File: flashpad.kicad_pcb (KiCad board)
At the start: 2 copper layers, 61.2 x 65.3 mm, 23 parts, among them U1 ATmega328P-PU, U2 ATmega32A-PU

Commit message: rev2
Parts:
- removed BOOT: BOOT, Button_Switch_THT:SW_PUSH_6mm
- removed the C3 at (155.2, 110.2)
- removed C4, C5: 100n, Capacitor_THT:C_Disc_D5.0mm_W2.5mm_P2.50mm
- removed C6, C7: 22p, Capacitor_THT:C_Disc_D5.0mm_W2.5mm_P5.00mm
- removed ISP1: AVR-ISP-6, Connector_PinHeader_2.54mm:PinHeader_2x03_P2.54mm_Horizontal
- removed LED1: LED, LED_THT:LED_D3.0mm
- removed the R5 at (138.4, 114.0)
- removed RESET: RESET, Button_Switch_THT:SW_PUSH_6mm
- removed XTAL1: Crystal, Crystal:Crystal_HC49-4H_Vertical
- added ACT: LED, LED_THT:LED_D5.0mm, F.Cu at (150.7, 90.1)
- added AVR: AVR-ISP-10, Connector_PinHeader_2.54mm:PinHeader_2x05_P2.54mm_Vertical, F.Cu at (134.7, 143.2)
- added C1: 22p, Capacitor_THT:C_Disc_D5.0mm_W2.5mm_P5.00mm, F.Cu at (100.2, 83.8)
- added C10: 22p, Capacitor_THT:C_Disc_D5.0mm_W2.5mm_P5.00mm, F.Cu at (126.8, 111.1)
- added C11: 22p, Capacitor_THT:C_Disc_D5.0mm_W2.5mm_P5.00mm, F.Cu at (126.8, 127.1)
- added C8: 100n, Capacitor_THT:C_Disc_D5.0mm_W2.5mm_P2.50mm, F.Cu at (128.8, 71.0)
- added C9: 100n, Capacitor_THT:C_Disc_D5.0mm_W2.5mm_P2.50mm, F.Cu at (126.4, 84.8)
- added G***: LOGO, custom_parts:elmo, B.Cu at (102.3, 63.4)
- added G***: LOGO, custom_parts:oshw, F.Cu at (102.2, 63.3)
- added JP1: SelfProg, Connector_PinHeader_2.54mm:PinHeader_1x02_P2.54mm_Vertical, F.Cu at (151.1, 79.9)
- added JP2: SlowSCK, Connector_PinHeader_2.54mm:PinHeader_1x02_P2.54mm_Vertical, F.Cu at (151.0, 75.4)
- added PWR: LED, LED_THT:LED_D5.0mm, F.Cu at (142.2, 90.1)
- added R1: 10k, Resistor_THT:R_Axial_DIN0204_L3.6mm_D1.6mm_P7.62mm_Horizontal, F.Cu at (153.3, 61.0)
- added R10: 1.5K, Resistor_THT:R_Axial_DIN0204_L3.6mm_D1.6mm_P7.62mm_Horizontal, F.Cu at (135.6, 92.3)
- added R2: 270r, Resistor_THT:R_Axial_DIN0204_L3.6mm_D1.6mm_P7.62mm_Horizontal, F.Cu at (123.9, 92.3)
- added R3: 270r, Resistor_THT:R_Axial_DIN0204_L3.6mm_D1.6mm_P7.62mm_Horizontal, F.Cu at (129.6, 92.3)
- added R9: 1.5K, Resistor_THT:R_Axial_DIN0204_L3.6mm_D1.6mm_P7.62mm_Horizontal, F.Cu at (132.7, 92.3)
- added U1: ATmega8A-PU, Package_DIP:DIP-28_W7.62mm, F.Cu at (145.3, 74.2)
- added X1: 12Mhz, Crystal:Crystal_HC49-4H_Vertical, F.Cu at (105.6, 80.0)
- added X2: 16Mhz, Crystal:Crystal_HC49-4H_Vertical, F.Cu at (129.4, 116.7)
- C2: value 100n -> 22p; footprint Capacitor_THT:C_Disc_D5.0mm_W2.5mm_P2.50mm -> Capacitor_THT:C_Disc_D5.0mm_W2.5mm_P5.00mm
- R4: value 1.5K -> 270r
- R5: renamed from R1; value 1.5K -> 2.2k
- U2: footprint Package_DIP:DIP-40_W15.24mm_Socket -> Socket:DIP_Socket-40_W11.9_W12.7_W15.24_W17.78_W18.5_3M_240-1280-00-0602J
- U3: renamed from U1; footprint Package_DIP:DIP-28_W7.62mm_Socket -> custom_parts:DIP_Socket-28_flipped
- USB1: value USB_B_Mini -> USB_B; footprint custom_parts:USB_Mini -> Connector_USB:USB_B_OST_USB-B1HSxx_Horizontal
- moved C2 54.6 mm to (100.2, 71.3)
- moved U3 47.1 mm to (152.8, 138.7), turned to 180 degrees
- moved R4 40.5 mm to (126.8, 92.3), turned to 270 degrees
- moved R6 36.8 mm to (150.5, 61.0)
- moved R5 35.4 mm to (145.0, 68.6)
- moved F1 35.4 mm to (110.9, 62.5), turned to 0 degrees
- moved C3 35.0 mm to (113.6, 67.4), turned to 270 degrees
- moved R7 34.5 mm to (147.7, 61.0)
- moved D2 32.2 mm to (142.0, 68.7)
- moved D1 32.0 mm to (138.8, 68.7)
- moved USB1 15.0 mm to (125.5, 64.7), turned to 90 degrees
- moved U2 1.56 mm to (116.2, 141.7)
- renumbered C1 to C3, R2 to R6, R3 to R7
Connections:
- net XTAL1 renamed XTAL2_1
- net XTAL2 renamed XTAL2_2
- C2 pad 1: +5V -> XTAL1_2
- R4 pad 1: RESET -> Net-(R4-Pad1)
- R4 pad 2: +5V -> SCK
- U2 pad 16: D+ -> Net-(U2-Pad16)
- U2 pad 17: D- -> Net-(U2-Pad17)
- U2 pad 18: BOOT -> Net-(U2-Pad18)
- U2 pad 5: MOSI -> Net-(U2-Pad5)
- U2 pad 6: MISO -> MOSI
- U2 pad 7: SCK -> MISO
- U2 pad 8: Net-(U2-Pad8) -> SCK
- U3 pad 4: D+ -> Net-(U3-Pad4)
- U3 pad 5: D- -> Net-(U3-Pad5)
- U3 pad 6: BOOT -> Net-(U3-Pad6)
- USB1 pad 4: Net-(USB1-Pad4) -> GND
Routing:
- net +5V: track 143.7 -> 259.3 mm
- net BOOT: track 103.5 -> 0.00 mm
- net MISO: track 89.0 -> 169.8 mm
- net Net-(JP1-Pad1): track 0.00 -> 41.5 mm
- net MOSI: track 94.1 -> 135.5 mm
- net RESET: track 93.7 -> 132.8 mm
- net SCK: track 87.3 -> 120.0 mm
- net XTAL1_1: track 0.00 -> 28.9 mm
- net XTAL1_2: track 0.00 -> 27.3 mm
- net LED2: track 0.00 -> 24.0 mm
- net Net-(LED2-Pad1): track 0.00 -> 20.0 mm
- net Net-(R3-Pad1): track 0.00 -> 17.7 mm
- net D-: track 29.8 -> 47.1 mm
- net D+: track 30.6 -> 47.7 mm
- net LED1: track 0.00 -> 16.8 mm
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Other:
- board size 61.2 x 65.3 mm -> 61.3 x 101.4 mm
- rule pad_to_mask_clearance: 0.05 -> 0
- board text added: "USBasp MultiPad by kb-elmo github.com/kb_elmo"

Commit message: update
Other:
- board text added: "USBasp MultiPad by kb-elmo github.com/kb-elmo"
- board text removed: "USBasp MultiPad by kb-elmo github.com/kb_elmo"

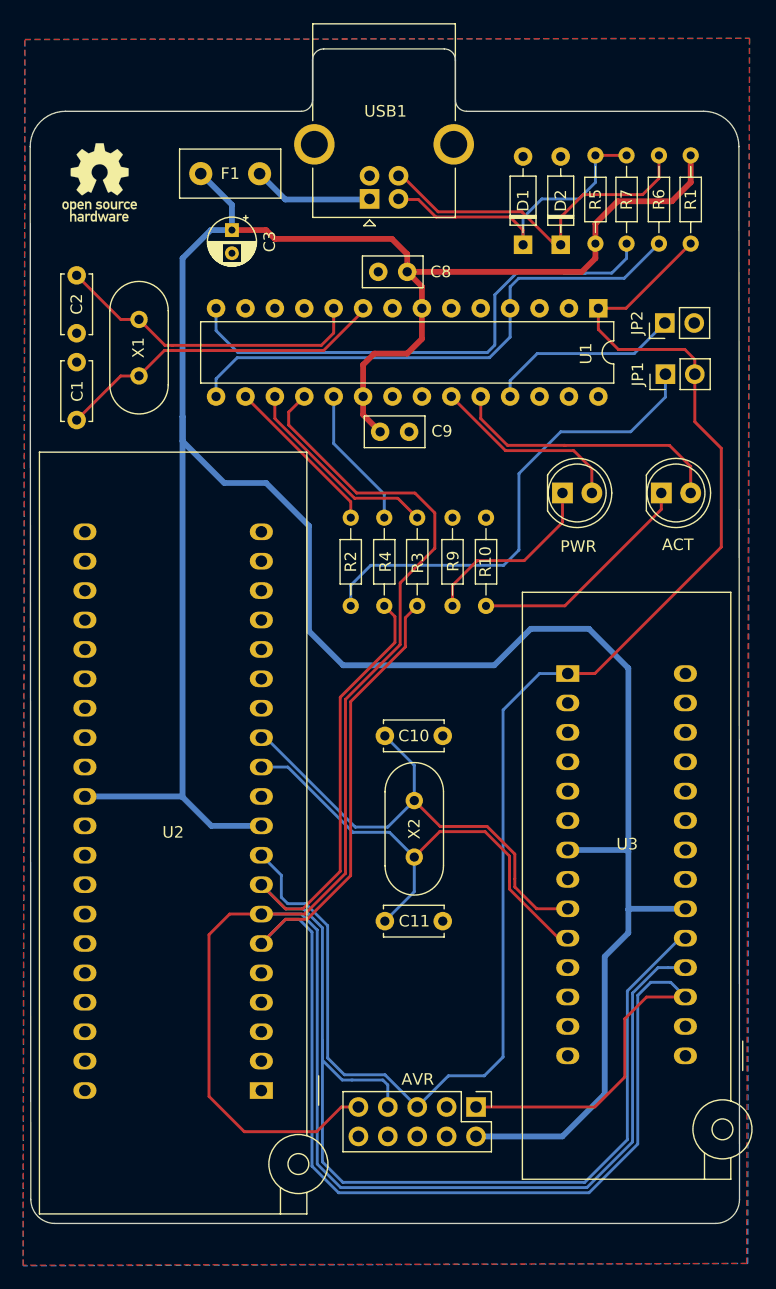
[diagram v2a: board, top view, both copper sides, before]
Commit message: fix footprints
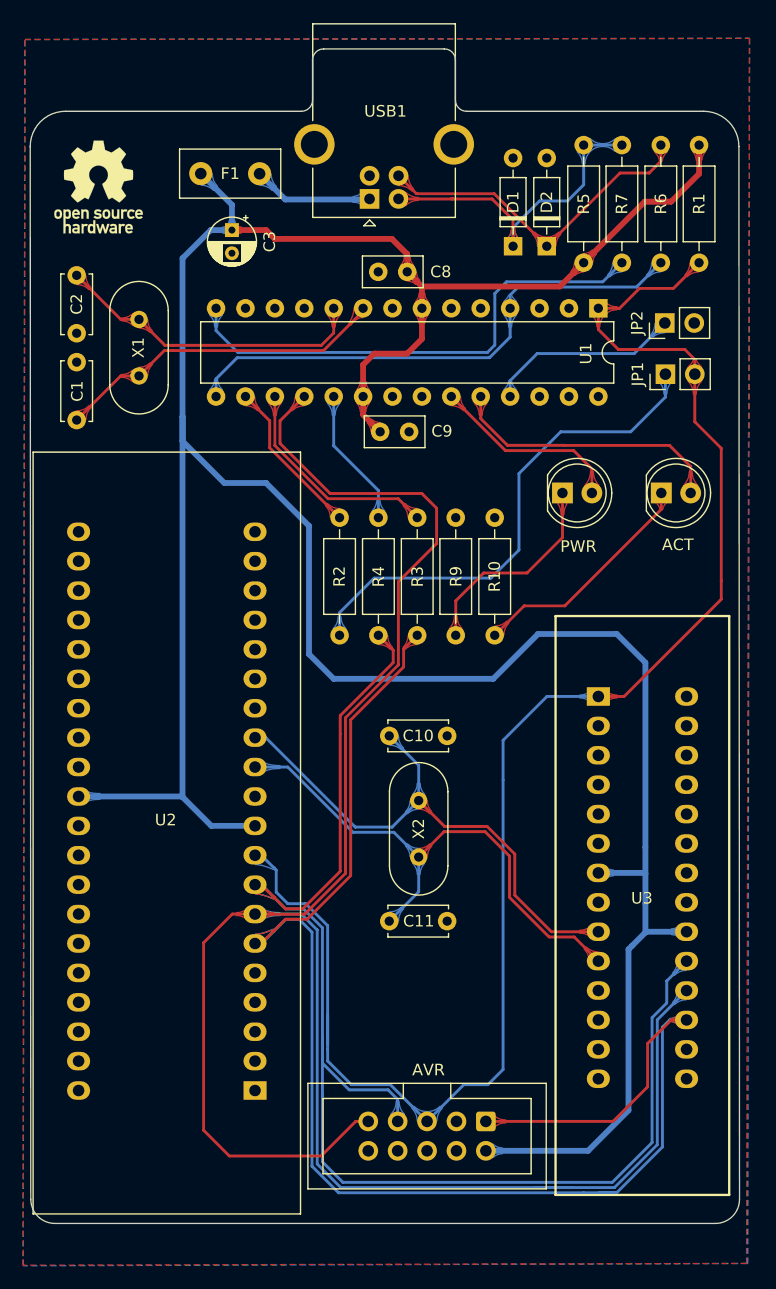
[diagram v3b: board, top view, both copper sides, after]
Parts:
- removed the AVR at (134.7, 143.2)
- removed the G*** at (102.2, 63.3)
- added AVR: AVR-ISP-10, Connector_IDC:IDC-Header_2x05_P2.54mm_Vertical, F.Cu at (135.6, 144.4)
- added REF**: OSHW-Logo_7.5x8mm_SilkScreen, Symbol:OSHW-Logo_7.5x8mm_SilkScreen, F.Cu at (102.1, 63.7)
- R1, R10, R2, R3, R4, R5, R6, R7, R9: footprint Resistor_THT:R_Axial_DIN0204_L3.6mm_D1.6mm_P7.62mm_Horizontal -> Resistor_THT:R_Axial_DIN0207_L6.3mm_D2.5mm_P10.16mm_Horizontal
- U2: footprint Socket:DIP_Socket-40_W11.9_W12.7_W15.24_W17.78_W18.5_3M_240-1280-00-0602J -> custom_parts:socket40dip
- U3: footprint custom_parts:DIP_Socket-28_flipped -> custom_parts:socket28dip
- moved U3 32.3 mm to (144.0, 107.7), turned to 0 degrees
- moved R5 1.94 mm to (144.0, 70.2)
- moved D2 1.21 mm to (140.8, 68.8)
- moved R1 1.15 mm to (154.0, 60.1)
- moved R7 0.98 mm to (147.3, 60.1)
- moved R2 0.97 mm to (122.9, 92.3)
- moved R6 0.90 mm to (150.7, 60.1)
- moved D1 0.87 mm to (137.9, 68.8)
- moved R10 0.75 mm to (136.3, 92.3)
- moved U2 0.55 mm to (115.6, 141.7)
- moved G*** 0.55 mm to (102.5, 63.9)
- moved R4 0.51 mm to (126.3, 92.3)
- moved C10 0.38 mm to (127.2, 111.1)
- moved C11 0.38 mm to (127.2, 127.1)
- moved X2 0.38 mm to (129.8, 116.7)
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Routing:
- net MISO: track 169.8 -> 177.7 mm
- net MOSI: track 135.5 -> 129.4 mm
- net RESET: track 132.8 -> 138.3 mm
- net XTAL2_2: track 42.7 -> 46.5 mm
- net XTAL2_1: track 42.8 -> 46.7 mm
- net D-: track 47.1 -> 43.6 mm
- net Net-(LED1-Pad1): track 16.1 -> 18.3 mm
- net Net-(JP1-Pad1): track 41.5 -> 43.7 mm
- net +5V: track 259.3 -> 261.2 mm
- net SCK: track 120.0 -> 121.7 mm
- net D+: track 47.7 -> 46.2 mm
- net Net-(R3-Pad1): track 17.7 -> 19.1 mm
- net Net-(D1-Pad1): track 28.0 -> 29.1 mm
- net Net-(D2-Pad1): track 30.7 -> 29.6 mm

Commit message: fix prototype issues
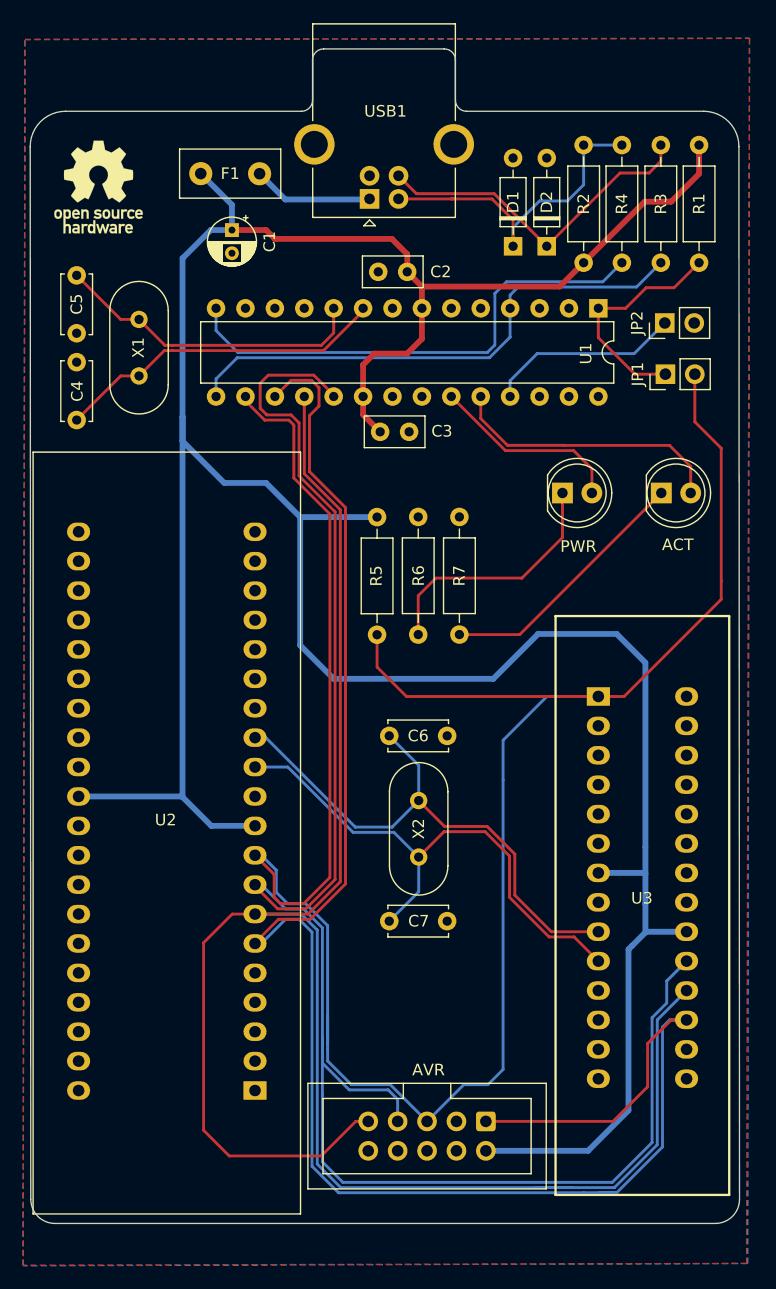
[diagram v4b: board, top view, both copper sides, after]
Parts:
- removed the R2 at (122.9, 92.3)
- removed the R3 at (129.6, 92.3)
- removed the R4 at (126.3, 92.3)
- added R5: 10k, Resistor_THT:R_Axial_DIN0207_L6.3mm_D2.5mm_P10.16mm_Horizontal, F.Cu at (126.2, 102.4)
- R2: renamed from R5; value 2.2k -> 1.5k
- moved R6 3.24 mm to (129.7, 92.2)
- moved R7 3.05 mm to (133.3, 92.2)
- renumbered C3 to C1, C8 to C2, C9 to C3, C1 to C4, C2 to C5, C10 to C6, C11 to C7, R6 to R3, R7 to R4, R9 to R6, R10 to R7
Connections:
- R1 pad 2: RESET -> Net-(JP1-Pad1)
- U1 pad 1: RESET -> Net-(JP1-Pad1)
- U1 pad 16: Net-(R2-Pad1) -> RESET
- U1 pad 17: Net-(R3-Pad1) -> MOSI
- U1 pad 19: Net-(R4-Pad1) -> SCK
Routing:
- net RESET: track 138.3 -> 194.5 mm
- net SCK: track 121.7 -> 153.1 mm
- net MOSI: track 129.4 -> 155.3 mm
- net Net-(JP1-Pad1): track 43.7 -> 20.0 mm
- net Net-(R3-Pad1): track 19.1 -> 0.00 mm
- net Net-(R2-Pad1): track 13.8 -> 0.00 mm
- net MISO: track 177.7 -> 164.6 mm
- net Net-(R4-Pad1): track 12.1 -> 0.00 mm
- net +5V: track 261.2 -> 267.9 mm
- net Net-(LED1-Pad1): track 18.3 -> 21.7 mm
- net Net-(LED2-Pad1): track 20.3 -> 22.5 mm
